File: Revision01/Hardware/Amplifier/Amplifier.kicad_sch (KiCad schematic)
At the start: 12 parts, among them U1 INA333AIDGKR, U2 TLV9061SQDBVRQ1

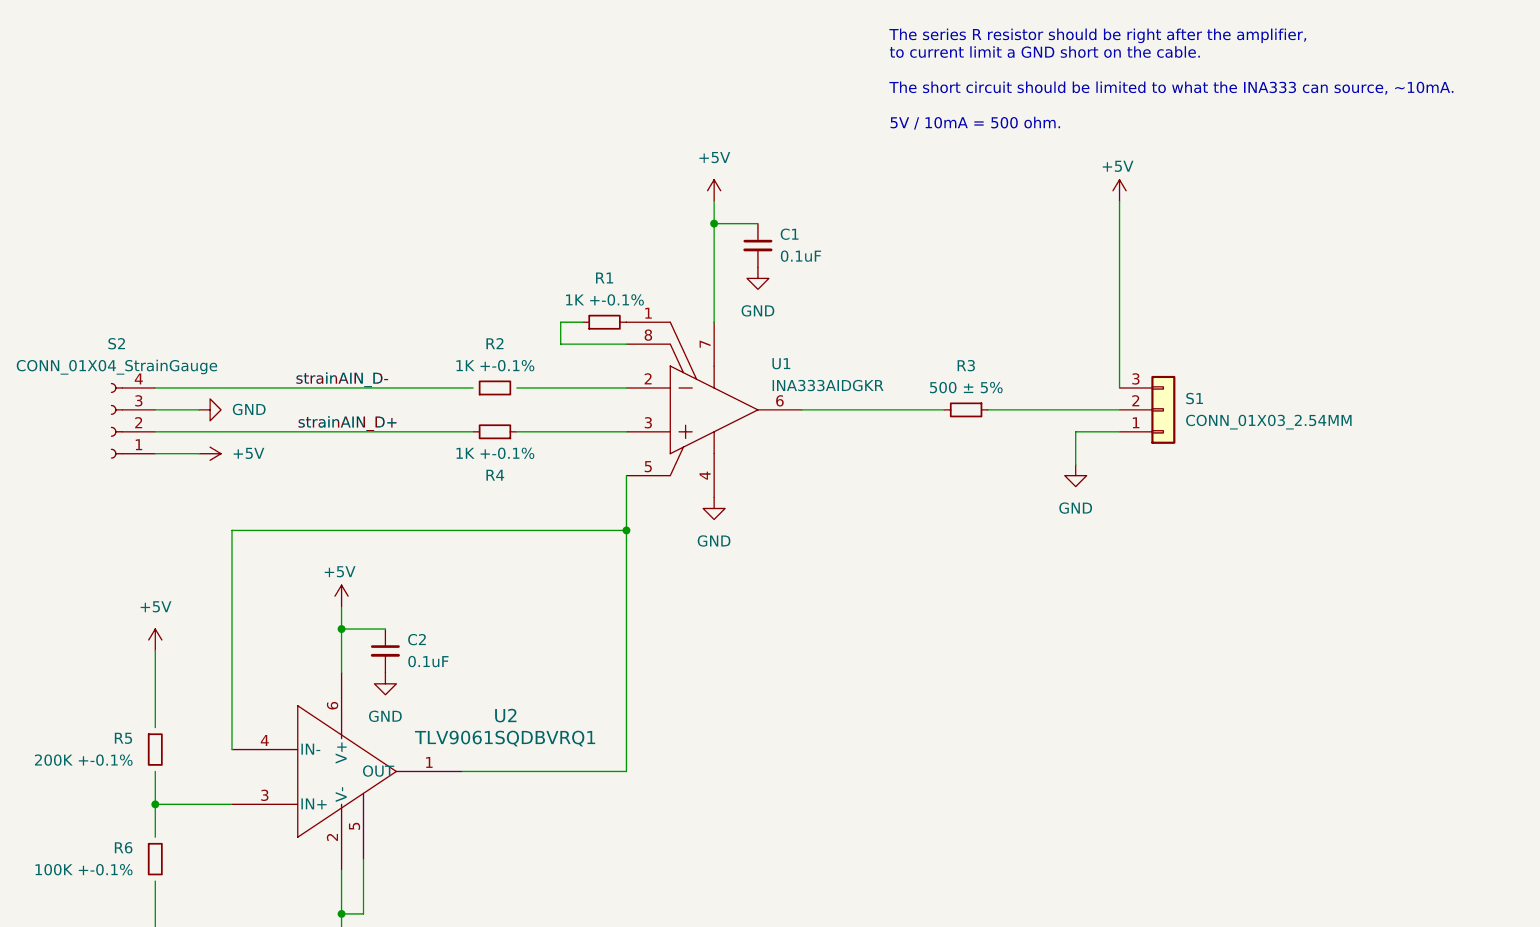
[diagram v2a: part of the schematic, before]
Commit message: . Merged Amplifier & Hub libraries into "Lib" . Added Amplifier 6 pin IDC footprint . Finalized Amplifier layout & silkscreen
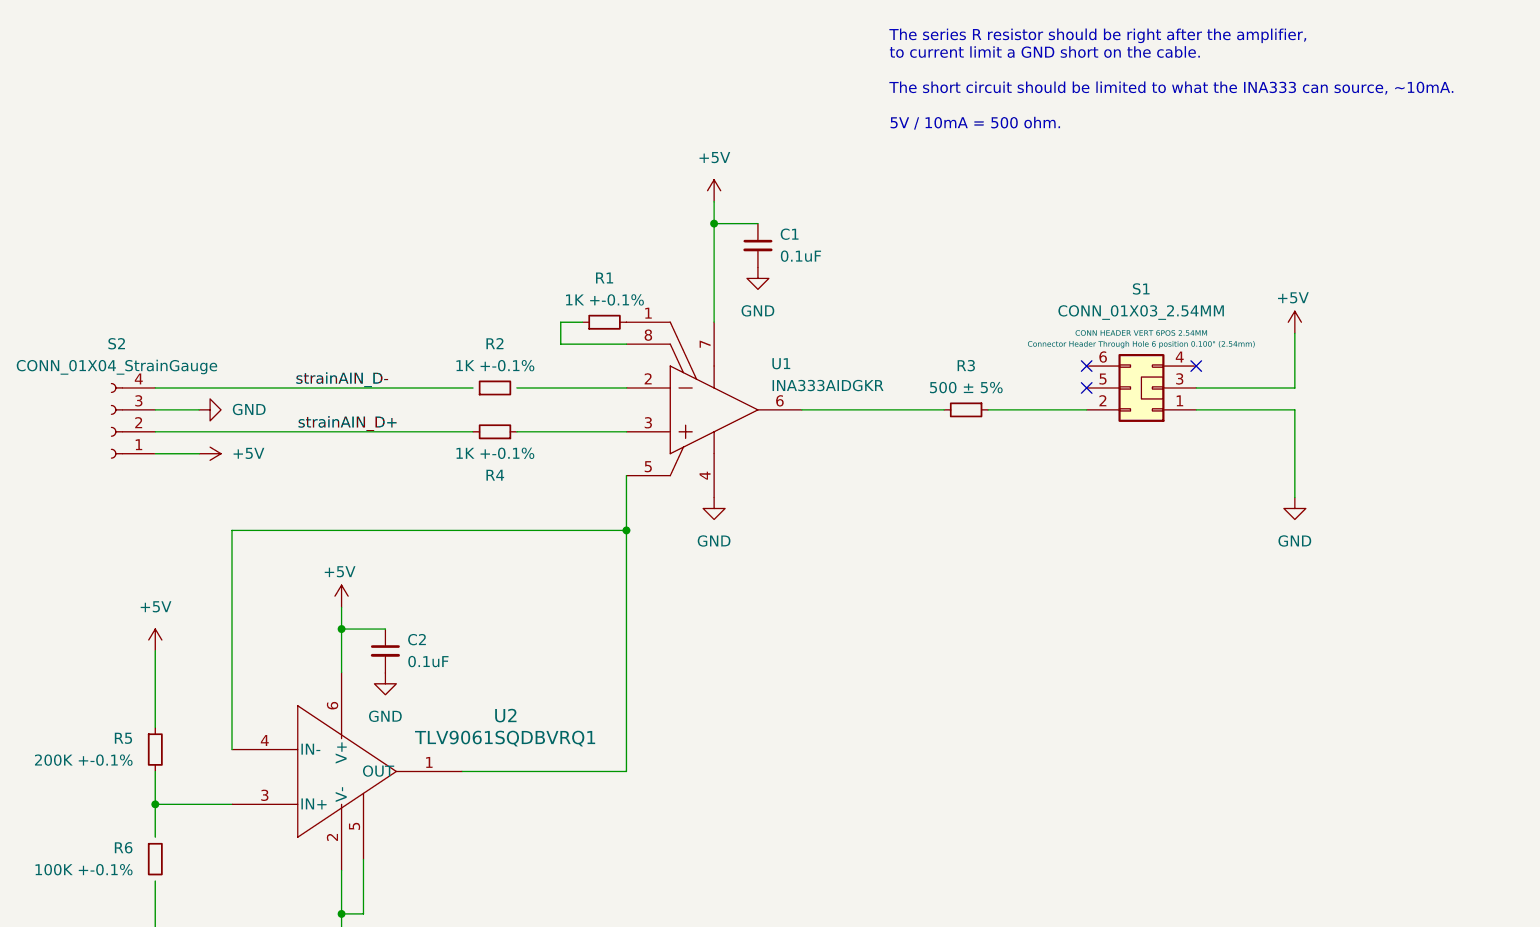
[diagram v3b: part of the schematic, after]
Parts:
- S1: footprint Connector_PinHeader_2.54mm:PinHeader_1x03_P2.54mm_Vertical -> Lib:AdamTech_BHR-06-VUA; symbol Connector_Generic:Conn_01x03 -> Lib:IDC_6Pin_Male_Header; Detailed Description (none) -> Connector Header Through Hole 6 position 0.100" (2.54mm); Distributor Link (none) -> https://www.digikey.ca/en/products/detail/adam-tech/BHR-06-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; Distributor Part Number (none) -> 2057-BHR-06-VUA-ND; Manufacturer (none) -> Adam Tech; Manufacturer Part Number (none) -> BHR-06-VUA
- S2: footprint Amplifier:CONN_01X04 -> Lib:CONN_01X04
- U1: footprint Amplifier:INA333AIDGKR_SOP65P490X110-8N -> Lib:INA333AIDGKR_SOP65P490X110-8N; symbol Amplifier:root_0_TI-INAXXXXXX8_Altium Content Vault -> Lib:root_0_TI-INAXXXXXX8_Altium Content Vault
- U2: symbol Amplifier:TLV9061SQDBVRQ1 -> Lib:TLV9061SQDBVRQ1
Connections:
- net +5V: now also R5.1
- net at U2.3 (IN+): now also R5.2
- no-connect marks 0 -> 3
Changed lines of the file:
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@@
 		(color 0 0 0 0)
 	)
+	(no_connect
+		(at 250.19 121.92)
+	)
+	(no_connect
+		(at 250.19 124.46)
+	)
+	(no_connect
+		(at 262.89 121.92)
+	)
 	(wire
 		(pts
@@
 	(wire
 		(pts
-			(xy 254 102.87) (xy 254 124.46)
+			(xy 274.32 118.11) (xy 274.32 124.46)
 		)
 		(stroke
@@
 	(wire
 		(pts
+			(xy 262.89 124.46) (xy 274.32 124.46)
+		)
+		(stroke
+			(width 0)
+			(type default)
+		)
+	)
+	(wire
+		(pts
 			(xy 163.83 187.96) (xy 163.83 185.42)
 		)
@@
 	(wire
 		(pts
-			(xy 238.76 127) (xy 254 127)
+			(xy 238.76 127) (xy 250.19 127)
 		)
 		(stroke
@@
 	(wire
 		(pts
-			(xy 248.92 129.54) (xy 248.92 133.35)
+			(xy 274.32 127) (xy 274.32 137.16)
 		)
 		(stroke
@@
 	(wire
 		(pts
-			(xy 248.92 129.54) (xy 254 129.54)
+			(xy 274.32 127) (xy 262.89 127)
 		)
 		(stroke
@@
 			)
 		)
-		(property "Footprint" "Amplifier:CONN_01X04"
+		(property "Footprint" "Lib:CONN_01X04"
 			(at 137.16 129.54 0)
 			(effects
@@
 	(symbol
 		(lib_id "power:+5V")
-		(at 254 102.87 0)
+		(at 274.32 118.11 0)
 		(unit 1)
 		(exclude_from_sim no)
@@
 		(dnp no)
 		(property "Reference" "#PWR04"
-			(at 254 106.68 0)
+			(at 274.32 121.92 0)
 			(effects
 				(font
@@
 		)
 		(property "Value" "+5V"
-			(at 253.746 98.806 0)
+			(at 274.066 114.046 0)
 			(effects
 				(font
@@
 		)
 		(property "Footprint" ""
-			(at 254 102.87 0)
+			(at 274.32 118.11 0)
 			(effects
 				(font
@@
 		)
 		(property "Datasheet" ""
-			(at 254 102.87 0)
+			(at 274.32 118.11 0)
 			(effects
 				(font
@@
 		)
 		(property "Description" "Power symbol creates a global label with name \"+5V\""
-			(at 254 102.87 0)
+			(at 274.32 118.11 0)
 			(effects
 				(font
@@
 		(lib_id "Device:R_Small")
 		(at 142.24 166.37 0)
-		(unit 0)
+		(unit 1)
 		(exclude_from_sim no)
 		(in_bom yes)
@@
 				(path "/a5b29326-90ee-4f27-a2a2-b00e145324d7"
 					(reference "R5")
-					(unit 0)
+					(unit 1)
 				)
 			)
@@
 	)
 	(symbol
-		(lib_id "Amplifier:TLV9061SQDBVRQ1")
+		(lib_id "Lib:TLV9061SQDBVRQ1")
 		(at 151.13 166.37 0)
 		(unit 1)
@@
 	)
 	(symbol
-		(lib_id "Connector_Generic:Conn_01x03")
-		(at 259.08 127 0)
-		(mirror x)
+		(lib_id "Lib:IDC_6Pin_Male_Header")
+		(at 257.81 124.46 180)
 		(unit 1)
 		(exclude_from_sim no)
@@
 		(fields_autoplaced yes)
 		(property "Reference" "S1"
-			(at 261.62 125.7299 0)
+			(at 256.54 113.03 0)
 			(effects
 				(font
 					(size 1.27 1.27)
 				)
-				(justify left)
 			)
 		)
 		(property "Value" "CONN_01X03_2.54MM"
-			(at 261.62 128.2699 0)
+			(at 256.54 115.57 0)
 			(effects
 				(font
 					(size 1.27 1.27)
 				)
-				(justify left)
 			)
 		)
-		(property "Footprint" "Connector_PinHeader_2.54mm:PinHeader_1x03_P2.54mm_Vertical"
-			(at 259.08 127 0)
+		(property "Footprint" "Lib:AdamTech_BHR-06-VUA"
+			(at 257.81 124.46 0)
 			(effects
 				(font
@@
 			)
 		)
-		(property "Datasheet" "~"
-			(at 259.08 127 0)
+		(property "Datasheet" "https://app.adam-tech.com/products/download/data_sheet/203218/bhr-xx-vua-data-sheet.pdf"
+			(at 257.81 124.46 0)
+			(effects
+				(font
+					(size 1.27 1.27)
+				)
+				(hide yes)
+			)
+		)
+		(property "Description" "CONN HEADER VERT 6POS 2.54MM"
+			(at 256.54 118.11 0)
+			(effects
+				(font
+					(size 0.635 0.635)
+				)
+			)
+		)
+		(property "Distributor Part Number" "2057-BHR-06-VUA-ND"
+			(at 256.54 135.89 0)
+			(effects
+				(font
+					(size 1.27 1.27)
+				)
+				(hide yes)
+			)
+		)
+		(property "Detailed Description" "Connector Header Through Hole 6 position 0.100\" (2.54mm)"
+			(at 256.54 119.38 0)
+			(effects
+				(font
+					(size 0.635 0.635)
+				)
+			)
+		)
+		(property "Distributor Link" "https://www.digikey.ca/en/products/detail/adam-tech/BHR-06-VUA/10414837"
+			(at 257.81 124.46 0)
 			(effects
 				(font
@@
 			)
 		)
-		(property "Description" "Generic connector, single row, 01x03, script generated (kicad-library-utils/schlib/autogen/connector/)"
-			(at 259.08 127 0)
+		(property "Manufacturer" "Adam Tech"
+			(at 256.54 133.35 0)
+			(effects
+				(font
+					(size 1.27 1.27)
+				)
+				(hide yes)
+			)
+		)
+		(property "Manufacturer Part Number" "BHR-06-VUA"
+			(at 256.54 130.81 0)
 			(effects
 				(font
@@
 		(pin "1"
 		)
+		(pin "4"
+		)
+		(pin "5"
+		)
+		(pin "6"
+		)
 		(instances
 			(project ""
@@
 	)
 	(symbol
-		(lib_id "Amplifier:root_0_TI-INAXXXXXX8_Altium Content Vault")
+		(lib_id "Lib:root_0_TI-INAXXXXXX8_Altium Content Vault")
 		(at 201.93 121.92 0)
 		(unit 1)
@@
 			)
 		)
-		(property "Footprint" "Amplifier:INA333AIDGKR_SOP65P490X110-8N"
+		(property "Footprint" "Lib:INA333AIDGKR_SOP65P490X110-8N"
 			(at 201.93 121.92 0)
 			(effects
@@
 	(symbol
 		(lib_id "power:GND")
-		(at 248.92 133.35 0)
+		(at 274.32 137.16 0)
+		(mirror y)
 		(unit 1)
 		(exclude_from_sim no)
@@
 		(fields_autoplaced yes)
 		(property "Reference" "#PWR08"
-			(at 248.92 139.7 0)
+			(at 274.32 143.51 0)
 			(effects
 				(font
@@
 		)
 		(property "Value" "GND"
-			(at 248.92 138.43 0)
+			(at 274.32 142.24 0)
 			(effects
 				(font
@@
 		)
 		(property "Footprint" ""
-			(at 248.92 133.35 0)
+			(at 274.32 137.16 0)
 			(effects
 				(font
@@
 		)
 		(property "Datasheet" ""
-			(at 248.92 133.35 0)
+			(at 274.32 137.16 0)
 			(effects
 				(font
@@
 		)
 		(property "Description" "Power symbol creates a global label with name \"GND\" , ground"
-			(at 248.92 133.35 0)
+			(at 274.32 137.16 0)
 			(effects
 				(font

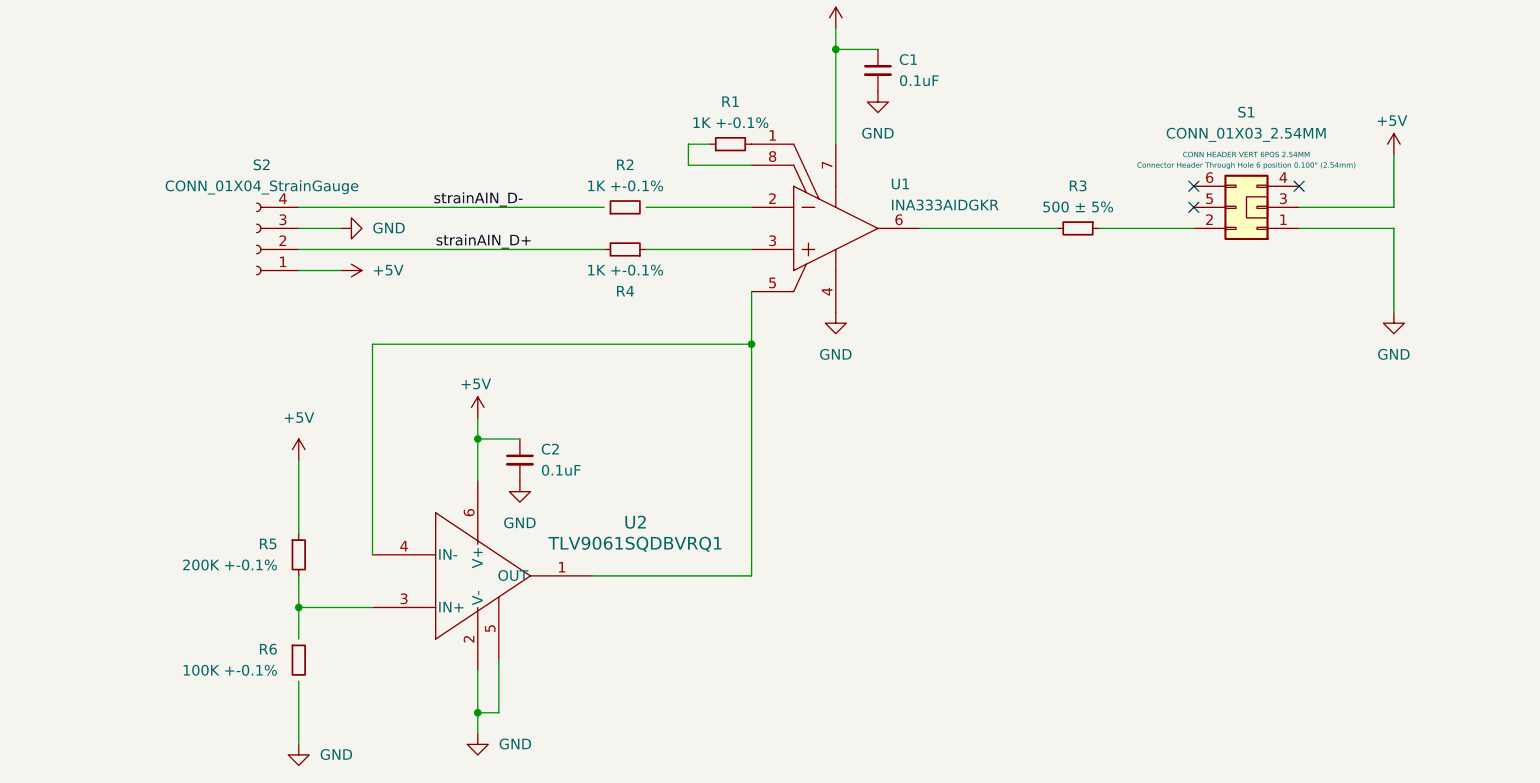
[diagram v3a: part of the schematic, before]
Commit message: . Amplifier: Changed 200K / 100K bias divider to 20K / 10K instead of placing a stability capacitor. . Amplifier: Found Mouser.ca components
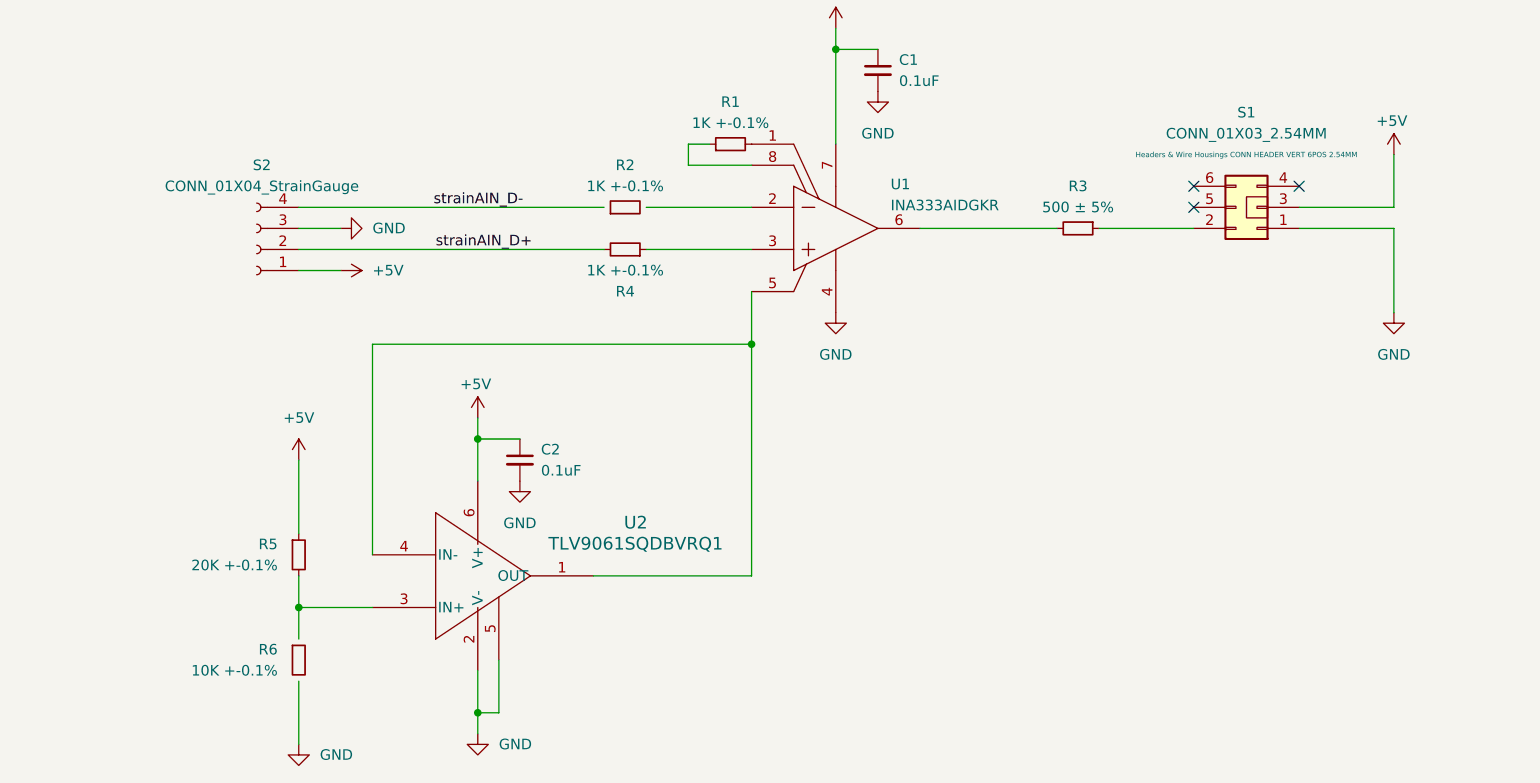
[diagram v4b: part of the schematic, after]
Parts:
- C1, C2: Manufacturer (none) -> Samsung Electro-Mechanics; Manufacturer Part Number (none) -> CL21B104KBCNNWC; Mouser Link (none) -> https://www.mouser.ca/ProductDetail/Samsung-Electro-Mechani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; Mouser Part Number (none) -> 187-CL21B104KBCNNWC; Package (none) -> 0805 (2012 Metric)
- R1, R2, R4: Manufacturer (none) -> Vishay / Beyschlag; Manufacturer Part Number (none) -> MCU08050D1001BP500; Mouser Link (none) -> https://www.mouser.ca/ProductDetail/Vishay-Beyschlag/MCU080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; Mouser Part Number (none) -> 594-MCU0805D1001BP5; Package (none) -> 0805 (2012 Metric)
- R3: Detailed Description 150 Ohms ±1% 0.125W, 1/8W Chip Resistor 0805 (2012 Metric) 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 -> (none); Distributor Link https://www.digikey.ca/en/products/detail/vishay-dale/CRCW0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 -> (none); Distributor Part Number 541-150CTR-ND -> (none); Manufacturer Vishay Dale -> Vishay / Beyschlag; Manufacturer Part Number CRCW0805150RFKEA -> MCU0805MD4990DP500; Mouser Link (none) -> https://www.mouser.ca/ProductDetail/Vishay-Beyschlag/MCU080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; Mouser Part Number (none) -> 594-MCU0805MD4990DP5
- R5: value 200K +-0.1% -> 20K +-0.1%; Manufacturer (none) -> Susumu; Manufacturer Part Number (none) -> RG2012P-203-B-T5; Mouser Link (none) -> https://www.mouser.ca/ProductDetail/Susumu/RG2012P-203-B-T5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; Mouser Part Number (none) -> 754-RG2012P-203-B-T5; Package (none) -> 0805 (2012 Metric)
- R6: value 100K +-0.1% -> 10K +-0.1%; Manufacturer (none) -> Susumu; Manufacturer Part Number (none) -> RG2012P-103-B-T5; Mouser Link (none) -> https://www.mouser.ca/ProductDetail/Susumu/RG2012P-103-B-T5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; Mouser Part Number (none) -> 754-RG2012P-103-B-T5; Package (none) -> 0805 (2012 Metric)
- S1: Detailed Description Connector Header Through Hole 6 position 0.100" (2.54mm) -> (none); Distributor Link https://www.digikey.ca/en/products/detail/adam-tech/BHR-06-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 -> (none); Distributor Part Number 2057-BHR-06-VUA-ND -> (none); Mouser Link (none) -> https://www.mouser.ca/ProductDetail/Adam-Tech/BHR-06-VUA?qs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; Mouser Part Number (none) -> 737-BHR-06-VUA
- S2: now left out of the parts list
- U1: Manufacturer (none) -> Texas Instruments; Manufacturer Part Number (none) -> INA333AIDGKR; Mouser Link (none) -> https://www.mouser.ca/ProductDetail/Texas-Instruments/INA33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; Mouser Part Number (none) -> 595-INA333AIDGKR; Package (none) -> VSSOP-8
- U2: Manufacturer (none) -> Texas Instruments; Manufacturer Part Number (none) -> TLV9061SQDBVRQ1; Mouser Link (none) -> https://www.mouser.ca/ProductDetail/Texas-Instruments/TLV90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; Mouser Part Number (none) -> 595-TLV9061SQDBVRQ1; Package (none) -> SOT-23-6
